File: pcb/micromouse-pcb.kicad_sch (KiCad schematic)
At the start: 61 parts, among them J1 Conn_01x08, J1_MotorEncoder1 Conn_01x06, J2_MotorEncoder1 Conn_01x06, J3 Conn_01x08, J4 Conn_01x08, Q1 BS170, Q2 TEFT4300, Q3 BS170, Q4 TEFT4300, Q5 BS170, Q6 TEFT4300, Q7 BS170, Q8 TEFT4300, Q9 FQP27P06, SW2 SW_SPDT, U1 Teensy_4.1, U2 L7805

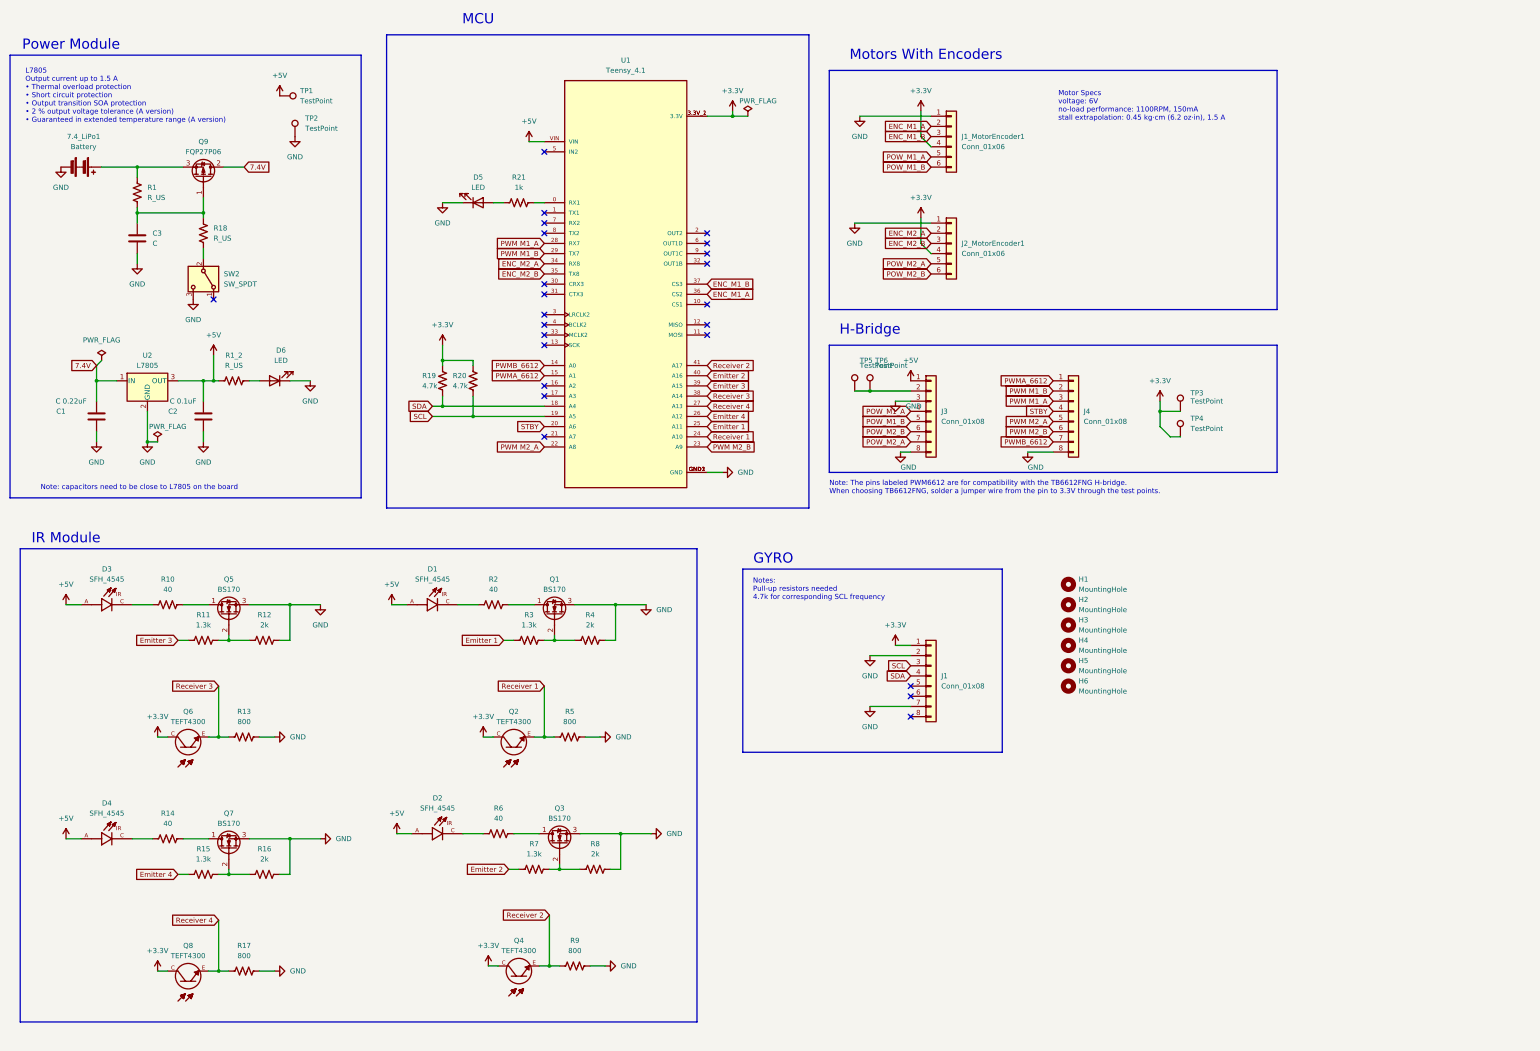
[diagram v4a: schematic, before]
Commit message: Added trim pots and DNP resistors
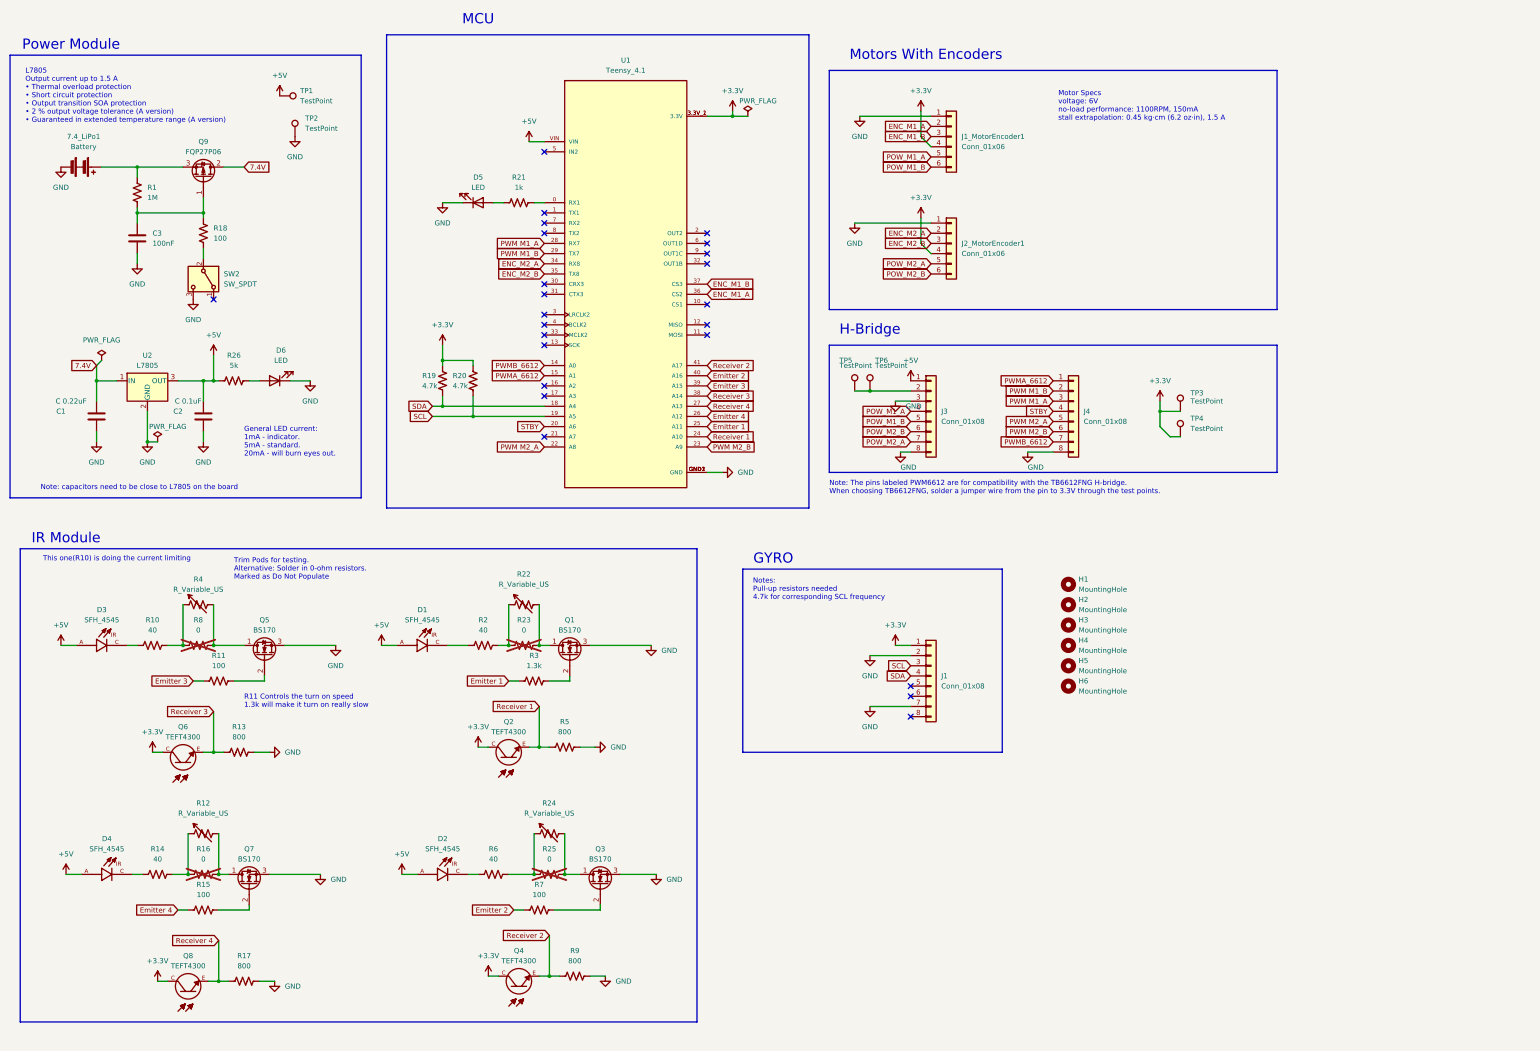
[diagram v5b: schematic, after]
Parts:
- removed R12, R4: 2k, Resistor_SMD:R_1206_3216Metric_Pad1.30x1.75mm_HandSolder, symbol Device:R_US
- added R12, R22, R24, R4: R_Variable_US, micromouse:TRIM_PV36W203C01B00, symbol Device:R_Variable_US
- added R23, R25: 0, Resistor_SMD:R_1206_3216Metric_Pad1.30x1.75mm_HandSolder, symbol Device:R_US
- C3: value C -> 100nF
- R1: value R_US -> 1M
- R11, R15, R7: value 1.3k -> 100
- R16, R8: value 2k -> 0; now not fitted
- R18: value R_US -> 100
- R26: renamed from R1_2; value R_US -> 5k
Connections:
- net GND: no longer R16.2, R8.2
- net at R2.2: now also R22.1, R23.1; no longer Q1.1 (D)
- net at Q3.2 (G), R7.2: no longer R8.1
- net at Q7.2 (G), R15.2: no longer R16.1
- net at R10.2: now also R8.1, R4.1; no longer Q5.1 (D)
- net at Q7.1 (D): now also R16.2, R12.2; no longer R14.2
- net at R6.2: now also R24.1, R25.1; no longer Q3.1 (D)
- new net: Q3.1 (D), R24.2, R25.2
- new net: R12.1, R14.2, R16.1
- new net: Q5.1 (D), R4.2, R8.2
- new net: Q1.1 (D), R22.2, R23.2
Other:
- note added: "General LED current: 1mA - indicator. 5mA - standard. 20mA - will burn eyes out."
- note added: "R11 Controls the turn on speed 1.3k will make it turn on really slow"
- note added: "This one(R10) is doing the current limiting"
- note added: "Trim Pods for testing. Alternative: Solder in 0-ohm resistors. Marked as Do Not Populate"
- moved on the sheet: D1, D2, D3, D4, Q1, Q2, Q3, Q4, Q5, Q6, Q7, Q8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

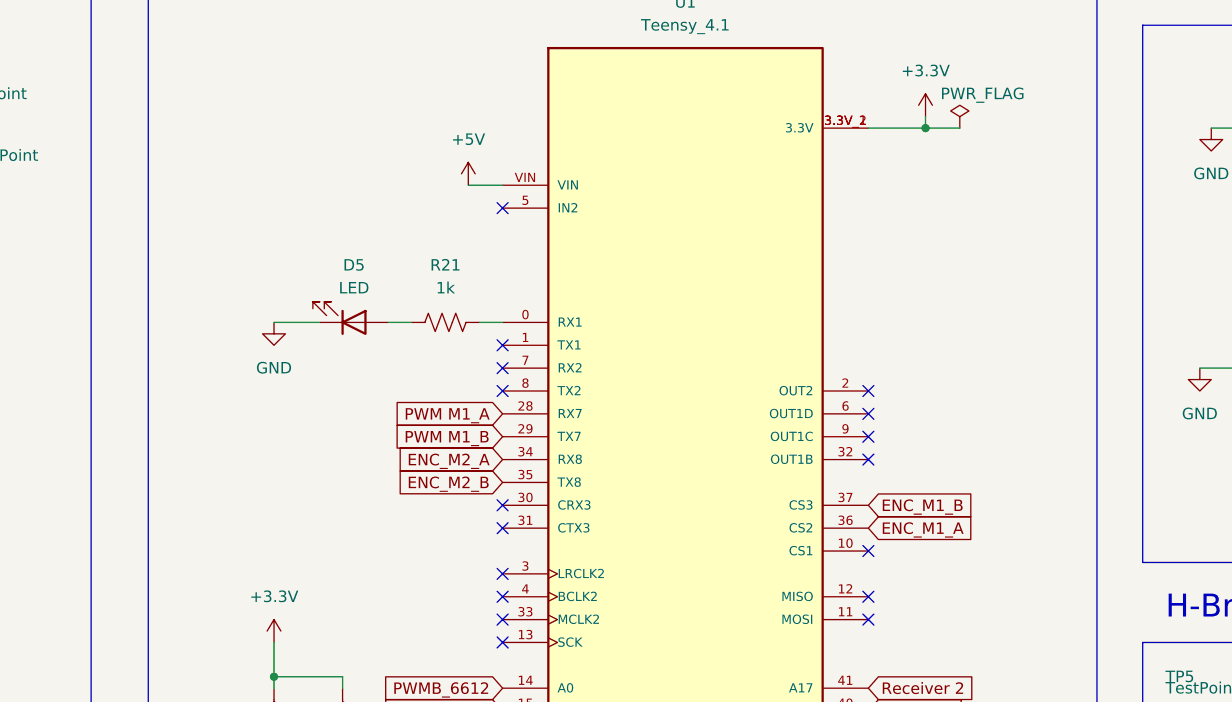
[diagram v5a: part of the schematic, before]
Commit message: updated pcb with buttons
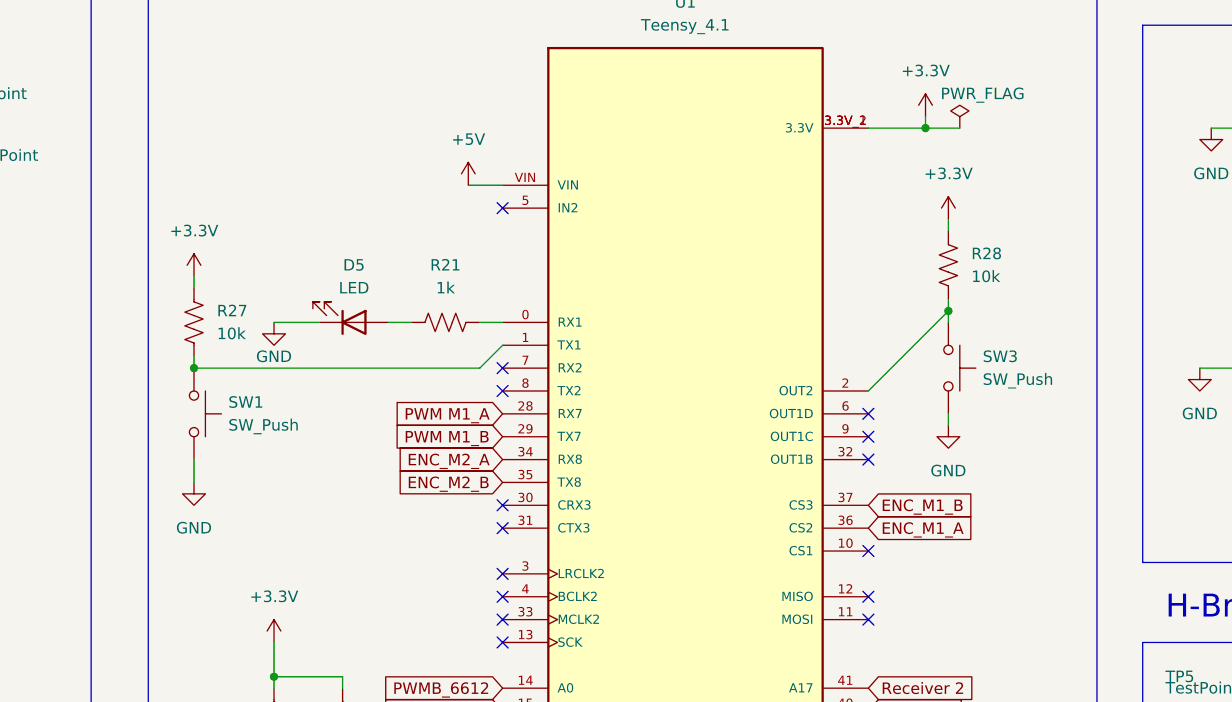
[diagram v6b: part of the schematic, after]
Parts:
- added R27, R28: 10k, Resistor_SMD:R_1206_3216Metric_Pad1.30x1.75mm_HandSolder, symbol Device:R_US
- added SW1, SW3: SW_Push, Button_Switch_SMD:SW_SPST_B3SL-1002P, symbol Switch:SW_Push
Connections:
- net +3.3V: now also R27.1, R28.1
- net GND: now also SW1.2, SW3.2
- net at U1.1 (TX1): now also R27.2, SW1.1
- net at U1.2 (OUT2): now also R28.2, SW3.1
- no-connect marks 24 -> 22

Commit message: Added Ratatoulli name
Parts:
- R3: value 1.3k -> 100
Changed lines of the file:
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@@
 			)
 		)
-		(property "Value" "1.3k"
+		(property "Value" "100"
 			(at 158.75 181.61 90)
 			(effects
